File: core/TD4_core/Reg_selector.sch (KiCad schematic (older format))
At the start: 2 parts, among them U37 74HC155

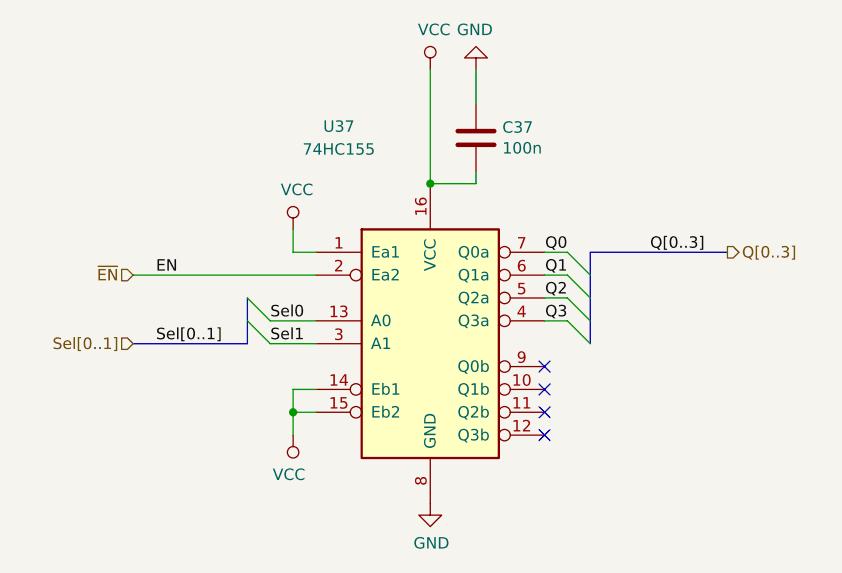
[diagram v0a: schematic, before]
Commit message: Core schematic done. Backplane connector added, including separate .sch file to append.
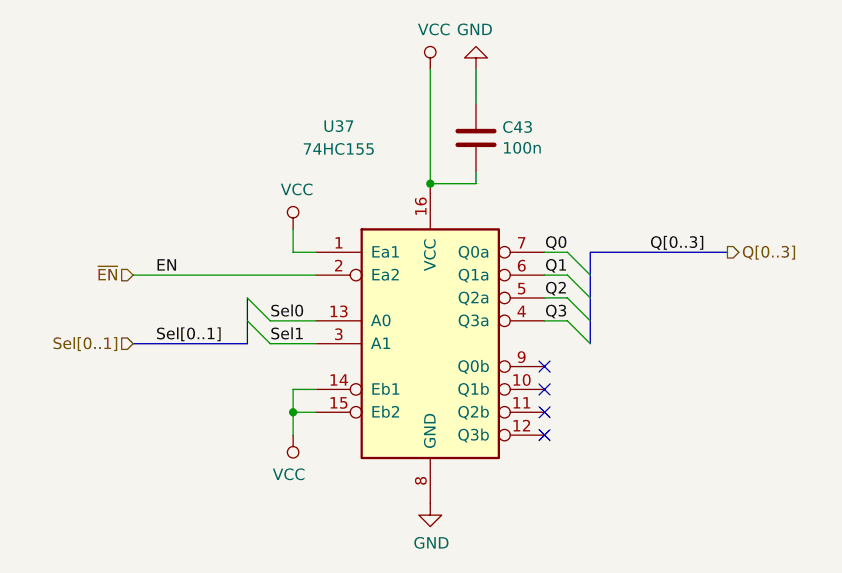
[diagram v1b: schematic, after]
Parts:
- C43: renamed from C37; footprint (none) -> Capacitor_SMD:C_0805_2012Metric
- U37: footprint (none) -> Package_SO:SOIC-16_3.9x9.9mm_P1.27mm
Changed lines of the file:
@@
 encoding utf-8
 Sheet 23 23
-Title ""
+Title "TD4 core module"
 Date ""
-Rev ""
+Rev "v1.0"
 Comp ""
 Comment1 ""
@@
 F 0 "U37" H 5300 4500 50  0000 C CNN
 F 1 "74HC155" H 5300 4400 50  0000 C CNN
-F 2 "" H 5700 3550 50  0001 C CNN
+F 2 "Package_SO:SOIC-16_3.9x9.9mm_P1.27mm" H 5700 3550 50  0001 C CNN
 F 3 "http://www.ti.com/lit/gpn/sn74LS155" H 5700 3550 50  0001 C CNN
 	1    5700 3550
@@
 	5900 2350 5900 2500
 $Comp
-L power:VCC #PWR0122
+L power:VCC #PWR0136
 U 1 1 5C64B718
 P 5700 2350
-F 0 "#PWR0122" H 5700 2200 50  0001 C CNN
+F 0 "#PWR0136" H 5700 2200 50  0001 C CNN
 F 1 "VCC" H 5717 2523 50  0000 C CNN
 F 2 "" H 5700 2350 50  0001 C CNN
@@
 $EndComp
 $Comp
-L power:GND #PWR0123
+L power:GND #PWR0137
 U 1 1 5C64B76A
 P 5900 2350
-F 0 "#PWR0123" H 5900 2100 50  0001 C CNN
+F 0 "#PWR0137" H 5900 2100 50  0001 C CNN
 F 1 "GND" H 5905 2177 50  0000 C CNN
 F 2 "" H 5900 2350 50  0001 C CNN
@@
 $EndComp
 $Comp
-L Device:C C37
+L Device:C C43
 U 1 1 5C64B5B6
 P 5900 2650
-F 0 "C37" H 6015 2696 50  0000 L CNN
+F 0 "C43" H 6015 2696 50  0000 L CNN
 F 1 "100n" H 6015 2605 50  0000 L CNN
-F 2 "" H 5938 2500 50  0001 C CNN
+F 2 "Capacitor_SMD:C_0805_2012Metric" H 5938 2500 50  0001 C CNN
 F 3 "~" H 5900 2650 50  0001 C CNN
 	1    5900 2650
@@
 	5700 2850 5900 2850
 $Comp
-L power:GND #PWR0126
+L power:GND #PWR0140
 U 1 1 5C64C0B6
 P 5700 4250
-F 0 "#PWR0126" H 5700 4000 50  0001 C CNN
+F 0 "#PWR0140" H 5700 4000 50  0001 C CNN
 F 1 "GND" H 5705 4077 50  0000 C CNN
 F 2 "" H 5700 4250 50  0001 C CNN
@@
 NoConn ~ 6200 3950
 $Comp
-L power:VCC #PWR0125
+L power:VCC #PWR0139
 U 1 1 5C64CAB9
 P 5100 3950
-F 0 "#PWR0125" H 5100 3800 50  0001 C CNN
+F 0 "#PWR0139" H 5100 3800 50  0001 C CNN
 F 1 "VCC" H 5118 4123 50  0000 C CNN
 F 2 "" H 5100 3950 50  0001 C CNN
@@
 	5100 3050 5100 3150
 $Comp
-L power:VCC #PWR0124
+L power:VCC #PWR0138
 U 1 1 5C64DEC3
 P 5100 3050
-F 0 "#PWR0124" H 5100 2900 50  0001 C CNN
+F 0 "#PWR0138" H 5100 2900 50  0001 C CNN
 F 1 "VCC" H 5117 3223 50  0000 C CNN
 F 2 "" H 5100 3050 50  0001 C CNN
